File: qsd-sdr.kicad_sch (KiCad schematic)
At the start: 51 parts, among them J11 SDR ANT, J12 SDR Out, U5 OPA1612AxD, U7 SN74CBT3253CDBR, U8 OPA1612AxD

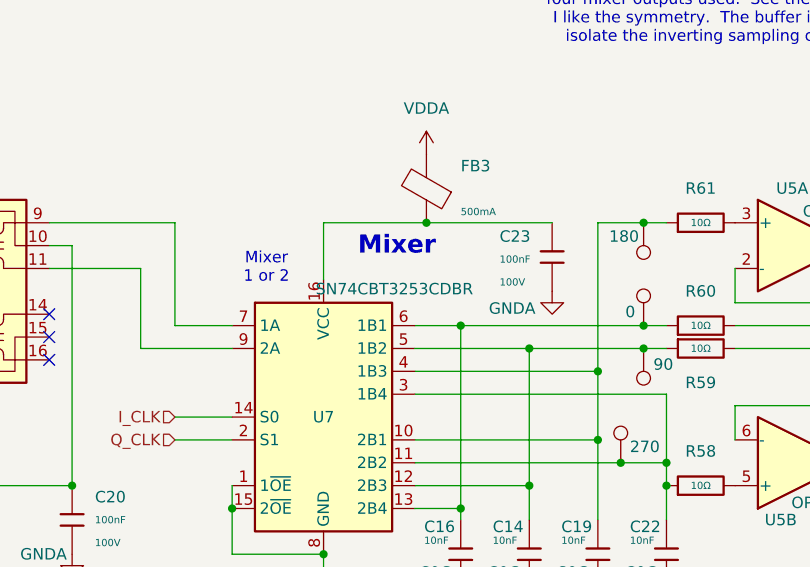
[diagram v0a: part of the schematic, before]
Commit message: Add .gbr to .gitignore
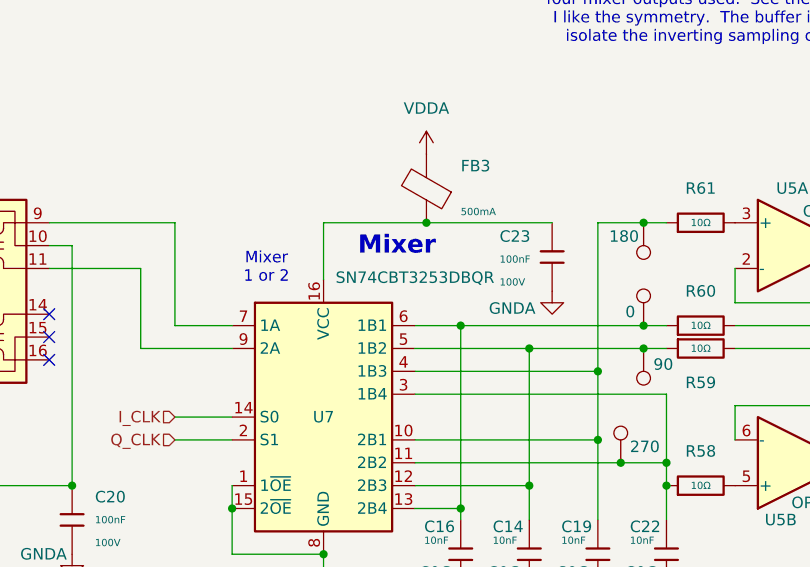
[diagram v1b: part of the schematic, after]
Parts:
- U7: value SN74CBT3253CDBR -> SN74CBT3253DBQR; footprint Package_SO:SSOP-16_3.9x4.9mm_P0.635mm -> Package_SO:SSOP-16_4.4x5.2mm_P0.65mm
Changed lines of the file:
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@@
 			)
 		)
-		(property "Value" "SN74CBT3253CDBR"
-			(at 138.684 79.756 0)
+		(property "Value" "SN74CBT3253DBQR"
+			(at 140.97 78.486 0)
 			(effects
 				(font
@@
 			)
 		)
-		(property "Footprint" "Package_SO:SSOP-16_3.9x4.9mm_P0.635mm"
+		(property "Footprint" "Package_SO:SSOP-16_4.4x5.2mm_P0.65mm"
 			(at 130.81 93.98 0)
 			(effects
@@
 			)
 		)
-		(property "Datasheet" "https://www.ti.com/cn/lit/gpn/sn74cbt3253c"
+		(property "Datasheet" ""
 			(at 130.81 93.98 0)
 			(effects

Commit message: Changed for Resubmission 2-27-2026
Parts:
- U7: footprint Package_SO:SSOP-16_4.4x5.2mm_P0.65mm -> Intro_to_CAD:DBQ0016A-IPC_A
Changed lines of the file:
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@@
 			)
 		)
-		(property "Footprint" "Package_SO:SSOP-16_4.4x5.2mm_P0.65mm"
+		(property "Footprint" "Intro_to_CAD:DBQ0016A-IPC_A"
 			(at 130.81 93.98 0)
 			(effects
@@
 			)
 		)
-		(property "Datasheet" ""
+		(property "Datasheet" "https://www.ti.com/lit/ds/symlink/sn74cbt3253c.pdf?ts=1772124766474&ref_url=https%253A%252F%252Fwww.ti.com%252Fproduct%252FSN74CBT3253C%252Fpart-details%252FSN74CBT3253CDBQR"
 			(at 130.81 93.98 0)
 			(effects

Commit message: Initial v0.2
Fixed SCL-SDA swap, 3V3 on encoder, and 3D models for Kicad 10
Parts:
- FB3: value ~ -> (none)

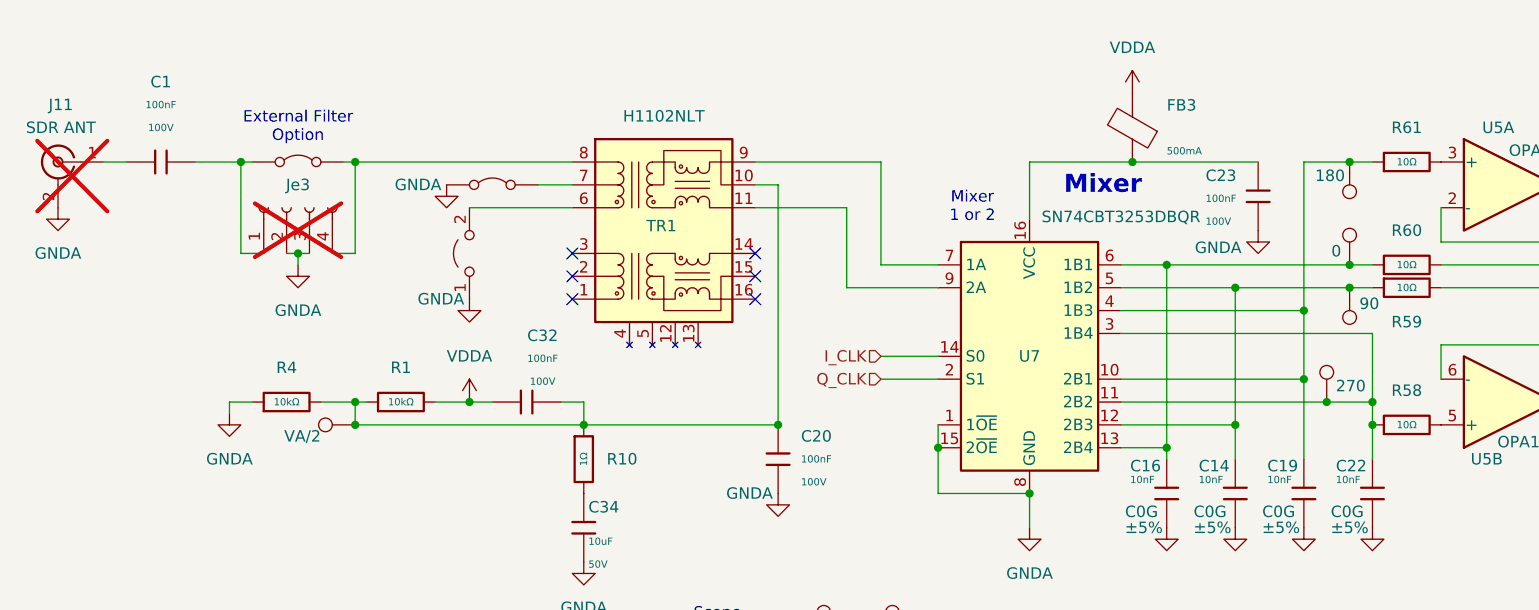
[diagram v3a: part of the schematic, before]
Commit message: Starting a new branch for v0.2
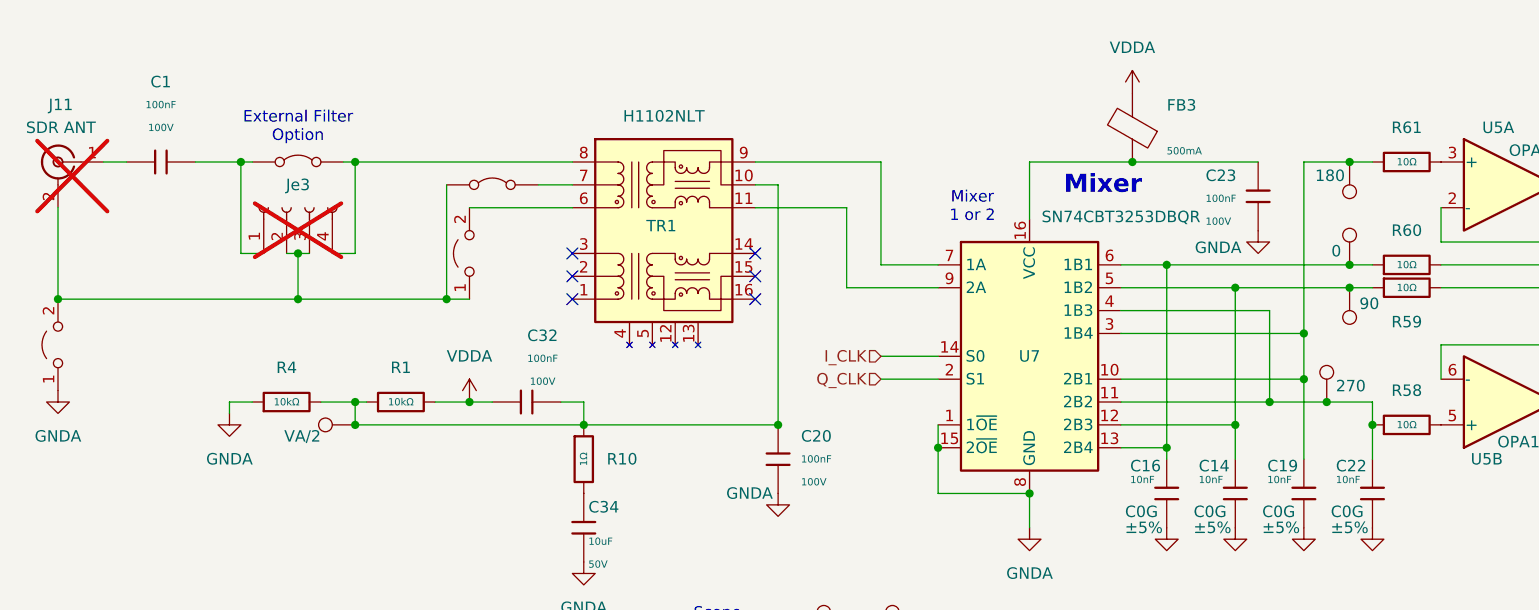
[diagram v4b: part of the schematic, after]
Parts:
- added JP89: GND_LP_SND, Jumper:SolderJumper-2_P1.3mm_Open_RoundedPad1.0x1.5mm, symbol Jumper:Jumper_2_Open
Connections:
- net GNDA: now also JP89.1 (A); no longer J11.2 (Ext), JP1.1 (A), JP88.1 (A), Je3.2 (Pin_2), Je3.3 (Pin_3)
- net at C19.1, R61.1, TP6.1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: now also U7.3 (1B4); no longer U7.4 (1B3)
- net at C22.1, R58.1, TP7.1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: now also U7.4 (1B3); no longer U7.3 (1B4)
- new net: J11.2 (Ext), JP1.1 (A), JP88.1 (A), JP89.2 (B), Je3.2 (Pin_2), Je3.3 (Pin_3)

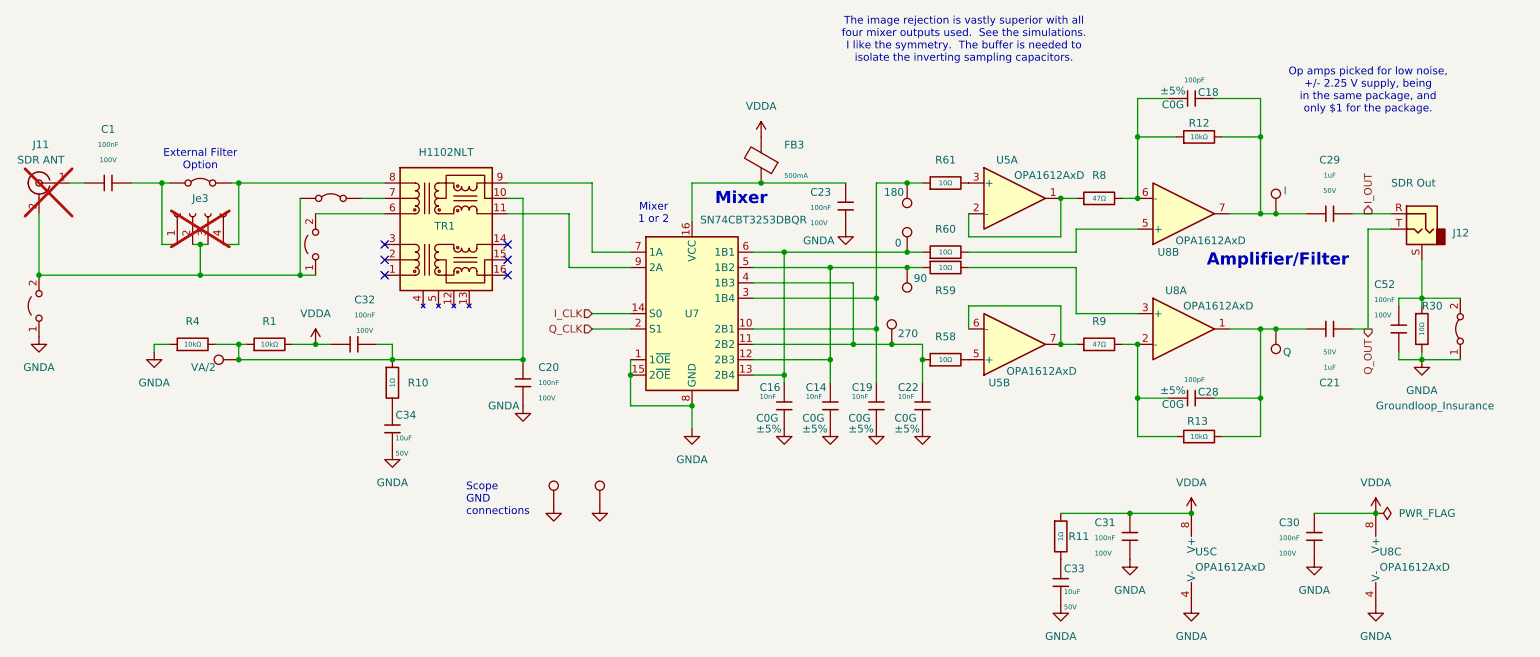
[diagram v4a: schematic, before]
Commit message: Adding fixes:
LDO for LO.  Reduce gain by 10/1.5.  Add better bypassing for VDDA/2 and CMOS Oscillator.  Added Johnson counter.  This is schematic only at the moment.
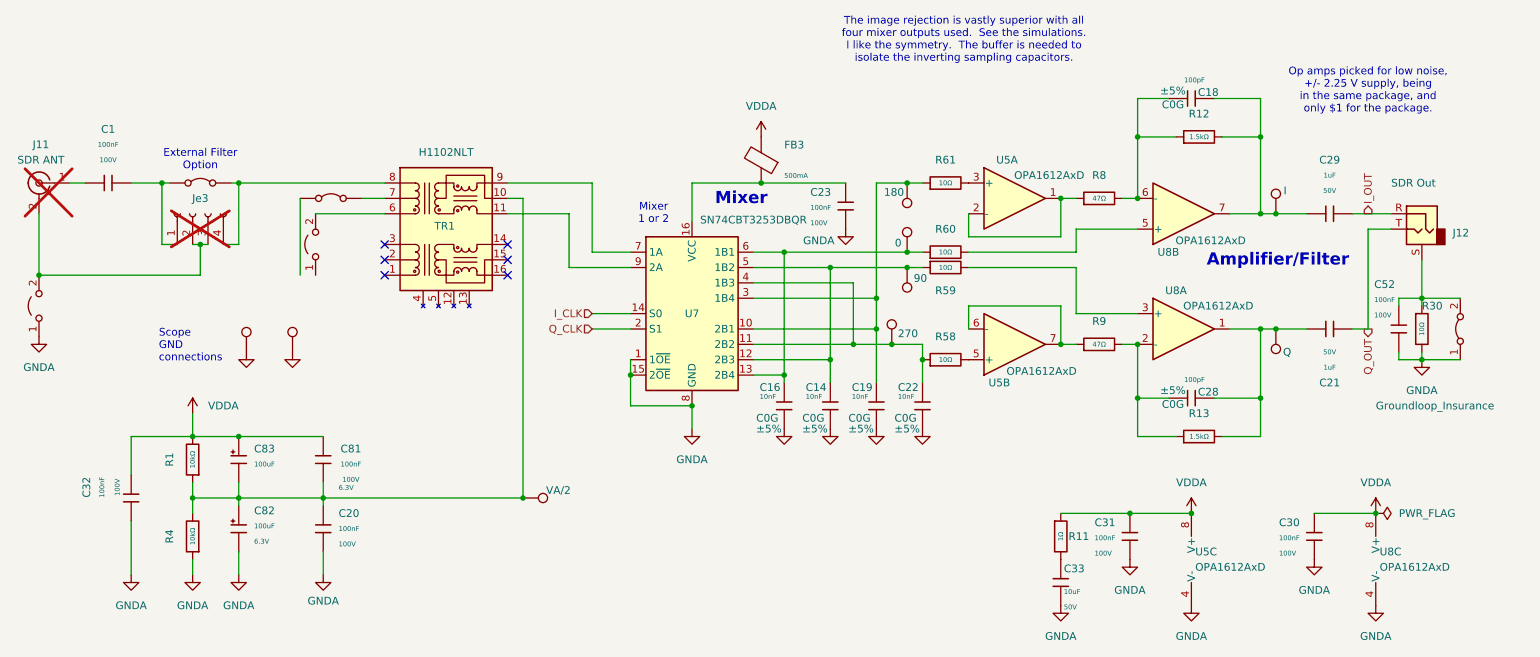
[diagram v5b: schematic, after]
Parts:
- removed C34: 10uF, PCM_JLCPCB:C_1206, symbol PCM_JLCPCB-Capacitors:1206,10uF
- removed R10: 1Ω, PCM_JLCPCB:R_0805, symbol PCM_JLCPCB-Resistors:0805,1Ω
- removed R12, R13: 10kΩ, PCM_JLCPCB:R_0805, symbol PCM_JLCPCB-Resistors:0805,10kΩ
- added C81: 100nF, PCM_JLCPCB:C_0805, symbol PCM_JLCPCB-Capacitors:0805,100nF
- added C82, C83: 100uF, PCM_JLCPCB:C_CASE-B-3528-21(mm), symbol PCM_JLCPCB-Capacitors:CASE-B-3528-21(mm),100uF
- added R12, R13: 1.5kΩ, PCM_JLCPCB:R_0805, symbol PCM_JLCPCB-Resistors:0805,1.5kΩ
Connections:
- net GNDA: now also C32.1, C82.2
- net VDDA: now also C32.2, C81.2, C83.1; no longer C32.1
- net at J11.2 (Ext), JP89.2 (B), Je3.2 (Pin_2)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: no longer JP1.1 (A), JP88.1 (A)
- net at C20.2, R1.1, R4.2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: now also C81.1, C82.1, C83.2; no longer C32.2
- net at C18.2, C29.1, TP17.1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: now also R12.2
- net at C18.1, R8.2, U8.6 (-): now also R12.1
- net at C28.1, R9.2, U8.2 (-): now also R13.1
- net at C21.2, C28.2, TP18.1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: now also R13.2
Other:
- moved on the sheet: C20, C32, R1, R4
